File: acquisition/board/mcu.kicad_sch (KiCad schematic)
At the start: 4 parts

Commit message: Continued initial design
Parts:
- gave numbers to parts that had none: 1
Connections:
- net D1V8: now reaches U7.1 (VDD)
- net D1V8: now also U7.17 (VDD), U7.5 (VDDA)
- net GND: now reaches U7.PAD (GND)
- net MCU_SPI_CS_N: now reaches U7.10 (PA4)
- net MCU_SPI_SCK: now reaches U7.11 (PA5)
- net MCU_SPI_SO: now reaches U7.12 (PA6)
- net MCU_SPI_SI: now reaches U7.13 (PA7)
- net ADC0_PDWN: now reaches U7.18 (PA8)
- net ADC1_PDWN: now reaches U7.19 (PA9)
- net ADC2_PDWN: now reaches U7.20 (PA10)
- net ADC3_PDWN: now reaches U7.21 (PA11)
- net PLL_SYNC: now reaches U7.22 (PA12)
- net PLL_SYNC: now also U7.6 (PA0)
- net SWD_SWDIO: now reaches U7.23 (PA13)
- net SWD_SCLK: now reaches U7.24 (PA14)
- net FPGA_INIT_B: now reaches U7.25 (PA15)
- net PLL_STATUS_LD: now reaches U7.7 (PA1)
- net UART_TX: now reaches U7.8 (PA2)
- net UART_TX: now also U7.9 (PA3)
- net PLL_STATUS_HOLDOVER: now reaches U7.14 (PB0)
- net PLL_STATUS_CLKIN0: now reaches U7.15 (PB1)
- net PLL_STATUS_CLKIN1: now reaches U7.16 (PB2)
- net FPGA_RST_N: now reaches U7.26 (PB3)
- net FPGA_DONE: now reaches U7.27 (PB4)
- net LED0: now reaches U7.28 (PB5)
- net LED1: now reaches U7.29 (PB6)
- net LED2: now reaches U7.30 (PB7)
- net LED3: now reaches U7.32 (PB8)
- no-connect marks 0 -> 2
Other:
- note added: "TODO: LEDs"
- note added: "TODO: decoupling"
- note added: "TODO: uart and swd debug headers"
- company: (none) -> A. Zonenberg
- title: (none) -> Digitizer board
- moved on the sheet: U7B, U7C, U7D
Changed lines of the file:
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@@
 (kicad_sch (version 20211123) (generator eeschema)
   (paper "A4")
-  (symbol (lib_id "st-azonenberg:STM32L031-QFN32") (at 101.6 97.79 0) (unit 3)
-    (in_bom yes) (on_board yes) (fields_autoplaced)
-    (property "Reference" "U?" (id 0) (at 117.5512 94.3415 0)
-      (effects (font (size 1.27 1.27)) (justify left))
-    )
-    (property "Value" "STM32L031-QFN32" (id 1) (at 117.5512 97.1166 0)
-      (effects (font (size 1.27 1.27)) (justify left))
-    )
-    (property "Footprint" "" (id 2) (at 101.6 97.79 0)
-      (effects (font (size 1.27 1.27)) hide)
-    )
-    (property "Datasheet" "" (id 3) (at 101.6 97.79 0)
+  (title_block
+    (title "Digitizer board")
+    (date "2022-06-22")
+    (rev "0.1")
+    (company "A. Zonenberg")
+  )
+  (junction (at 36.83 127) (diameter 0) (color 0 0 0 0)
+  )
+  (no_connect (at 36.83 114.3))
+  (no_connect (at 36.83 111.76))
+  (wire (pts (xy 36.83 123.19) (xy 36.83 127))
+    (stroke (width 0) (type default) (color 0 0 0 0))
+  )
+  (wire (pts (xy 36.83 127) (xy 36.83 129.54))
+    (stroke (width 0) (type default) (color 0 0 0 0))
+  )
+  (text "TODO: decoupling" (at 45.72 162.56 0)
+    (effects (font (size 1.27 1.27)) (justify left bottom))
+  )
+  (text "TODO: LEDs" (at 127 87.63 0)
+    (effects (font (size 1.27 1.27)) (justify left bottom))
+  )
+  (text "TODO: uart and swd debug headers" (at 72.39 158.75 0)
+    (effects (font (size 1.27 1.27)) (justify left bottom))
+  )
+  (label "SWD_SWDIO" (at 36.83 64.77 180)
+    (effects (font (size 1.27 1.27)) (justify right bottom))
+  )
+  (label "UART_RX" (at 113.03 55.88 0)
+    (effects (font (size 1.27 1.27)) (justify left bottom))
+  )
+  (label "LED3" (at 116.84 77.47 180)
+    (effects (font (size 1.27 1.27)) (justify right bottom))
+  )
+  (label "LED2" (at 116.84 74.93 180)
+    (effects (font (size 1.27 1.27)) (justify right bottom))
+  )
+  (label "UART_TX" (at 36.83 39.37 180)
+    (effects (font (size 1.27 1.27)) (justify right bottom))
+  )
+  (label "LED0" (at 116.84 69.85 180)
+    (effects (font (size 1.27 1.27)) (justify right bottom))
+  )
+  (label "LED2" (at 36.83 99.06 180)
+    (effects (font (size 1.27 1.27)) (justify right bottom))
+  )
+  (label "UART_TX" (at 36.83 36.83 180)
+    (effects (font (size 1.27 1.27)) (justify right bottom))
+  )
+  (label "LED3" (at 36.83 101.6 180)
+    (effects (font (size 1.27 1.27)) (justify right bottom))
+  )
+  (label "LED0" (at 36.83 93.98 180)
+    (effects (font (size 1.27 1.27)) (justify right bottom))
+  )
+  (label "UART_TX" (at 113.03 53.34 0)
+    (effects (font (size 1.27 1.27)) (justify left bottom))
+  )
+  (label "LED1" (at 116.84 72.39 180)
+    (effects (font (size 1.27 1.27)) (justify right bottom))
+  )
+  (label "SWD_SCLK" (at 36.83 67.31 180)
+    (effects (font (size 1.27 1.27)) (justify right bottom))
+  )
+  (label "LED1" (at 36.83 96.52 180)
+    (effects (font (size 1.27 1.27)) (justify right bottom))
+  )
+  (hierarchical_label "FPGA_DONE" (shape input) (at 36.83 91.44 180)
+    (effects (font (size 1.27 1.27)) (justify right))
+  )
+  (hierarchical_label "PLL_STATUS_LD" (shape input) (at 36.83 34.29 180)
+    (effects (font (size 1.27 1.27)) (justify right))
+  )
+  (hierarchical_label "PLL_SYNC" (shape output) (at 36.83 31.75 180)
+    (effects (font (size 1.27 1.27)) (justify right))
+  )
+  (hierarchical_label "FPGA_RST_N" (shape output) (at 36.83 88.9 180)
+    (effects (font (size 1.27 1.27)) (justify right))
+  )
+  (hierarchical_label "FPGA_INIT_B" (shape bidirectional) (at 36.83 69.85 180)
+    (effects (font (size 1.27 1.27)) (justify right))
+  )
+  (hierarchical_label "ADC0_PDWN" (shape output) (at 36.83 52.07 180)
+    (effects (font (size 1.27 1.27)) (justify right))
+  )
+  (hierarchical_label "ADC2_PDWN" (shape output) (at 36.83 57.15 180)
+    (effects (font (size 1.27 1.27)) (justify right))
+  )
+  (hierarchical_label "D1V8" (shape input) (at 36.83 123.19 180)
+    (effects (font (size 1.27 1.27)) (justify right))
+  )
+  (hierarchical_label "PLL_STATUS_CLKIN0" (shape input) (at 36.83 83.82 180)
+    (effects (font (size 1.27 1.27)) (justify right))
+  )
+  (hierarchical_label "PLL_SYNC" (shape output) (at 36.83 62.23 180)
+    (effects (font (size 1.27 1.27)) (justify right))
+  )
+  (hierarchical_label "MCU_SPI_CS_N" (shape output) (at 36.83 41.91 180)
+    (effects (font (size 1.27 1.27)) (justify right))
+  )
+  (hierarchical_label "PLL_STATUS_HOLDOVER" (shape input) (at 36.83 81.28 180)
+    (effects (font (size 1.27 1.27)) (justify right))
+  )
+  (hierarchical_label "ADC1_PDWN" (shape output) (at 36.83 54.61 180)
+    (effects (font (size 1.27 1.27)) (justify right))
+  )
+  (hierarchical_label "ADC3_PDWN" (shape output) (at 36.83 59.69 180)
+    (effects (font (size 1.27 1.27)) (justify right))
+  )
+  (hierarchical_label "MCU_SPI_SO" (shape input) (at 36.83 46.99 180)
+    (effects (font (size 1.27 1.27)) (justify right))
+  )
+  (hierarchical_label "MCU_SPI_SI" (shape output) (at 36.83 49.53 180)
+    (effects (font (size 1.27 1.27)) (justify right))
+  )
+  (hierarchical_label "MCU_SPI_SCK" (shape output) (at 36.83 44.45 180)
+    (effects (font (size 1.27 1.27)) (justify right))
+  )
+  (hierarchical_label "GND" (shape input) (at 36.83 134.62 180)
+    (effects (font (size 1.27 1.27)) (justify right))
+  )
+  (hierarchical_label "PLL_STATUS_CLKIN1" (shape input) (at 36.83 86.36 180)
+    (effects (font (size 1.27 1.27)) (justify right))
+  )
+  (symbol (lib_id "st-azonenberg:STM32L031-QFN32") (at 40.64 115.57 0) (unit 3)
+    (in_bom yes) (on_board yes)
+    (property "Reference" "U7" (id 0) (at 40.64 116.84 0)
+      (effects (font (size 1.27 1.27)) (justify left))
+    )
+    (property "Value" "STM32L031-QFN32" (id 1) (at 40.64 119.6151 0)
+      (effects (font (size 1.27 1.27)) (justify left))
+    )
+    (property "Footprint" "" (id 2) (at 40.64 115.57 0)
+      (effects (font (size 1.27 1.27)) hide)
+    )
+    (property "Datasheet" "" (id 3) (at 40.64 115.57 0)
       (effects (font (size 1.27 1.27)) hide)
     )
@@
     (pin "3")
   )
-  (symbol (lib_id "st-azonenberg:STM32L031-QFN32") (at 152.4 110.49 0) (unit 4)
-    (in_bom yes) (on_board yes) (fields_autoplaced)
-    (property "Reference" "U?" (id 0) (at 168.3512 98.7865 0)
-      (effects (font (size 1.27 1.27)) (justify left))
-    )
-    (property "Value" "STM32L031-QFN32" (id 1) (at 168.3512 101.5616 0)
-      (effects (font (size 1.27 1.27)) (justify left))
-    )
-    (property "Footprint" "" (id 2) (at 152.4 110.49 0)
-      (effects (font (size 1.27 1.27)) hide)
-    )
-    (property "Datasheet" "" (id 3) (at 152.4 110.49 0)
+  (symbol (lib_id "st-azonenberg:STM32L031-QFN32") (at 40.64 143.51 0) (unit 4)
+    (in_bom yes) (on_board yes)
+    (property "Reference" "U7" (id 0) (at 40.64 145.415 0)
+      (effects (font (size 1.27 1.27)) (justify left))
+    )
+    (property "Value" "STM32L031-QFN32" (id 1) (at 40.64 148.1901 0)
+      (effects (font (size 1.27 1.27)) (justify left))
+    )
+    (property "Footprint" "" (id 2) (at 40.64 143.51 0)
+      (effects (font (size 1.27 1.27)) hide)
+    )
+    (property "Datasheet" "" (id 3) (at 40.64 143.51 0)
       (effects (font (size 1.27 1.27)) hide)
     )
@@
   )
   (symbol (lib_id "st-azonenberg:STM32L031-QFN32") (at 40.64 71.12 0) (unit 1)
-    (in_bom yes) (on_board yes) (fields_autoplaced)
-    (property "Reference" "U?" (id 0) (at 56.5912 49.8915 0)
-      (effects (font (size 1.27 1.27)) (justify left))
-    )
-    (property "Value" "STM32L031-QFN32" (id 1) (at 56.5912 52.6666 0)
+    (in_bom yes) (on_board yes)
+    (property "Reference" "U7" (id 0) (at 40.64 72.1549 0)
+      (effects (font (size 1.27 1.27)) (justify left))
+    )
+    (property "Value" "STM32L031-QFN32" (id 1) (at 40.64 74.93 0)
       (effects (font (size 1.27 1.27)) (justify left))
     )
@@
       (effects (font (size 1.27 1.27)) hide)
     )
-    (pin "10")
-    (pin "11")
-    (pin "12")
-    (pin "13")
+    (pin "10" (alternate "SPI1_NSS"))
+    (pin "11" (alternate "SPI1_SCK"))
+    (pin "12" (alternate "SPI1_MISO"))
+    (pin "13" (alternate "SPI1_MOSI"))
     (pin "18")
     (pin "19")
@@
     (pin "21")
     (pin "22")
-    (pin "23")
-    (pin "24")
+    (pin "23" (alternate "SWDIO"))
+    (pin "24" (alternate "SWCLK"))
     (pin "25")
     (pin "6")
     (pin "7")
-    (pin "8")
-    (pin "9")
-  )
-  (symbol (lib_id "st-azonenberg:STM32L031-QFN32") (at 72.39 86.36 0) (unit 2)
-    (in_bom yes) (on_board yes) (fields_autoplaced)
-    (property "Reference" "U?" (id 0) (at 88.3412 74.0215 0)
-      (effects (font (size 1.27 1.27)) (justify left))
-    )
-    (property "Value" "STM32L031-QFN32" (id 1) (at 88.3412 76.7966 0)
-      (effects (font (size 1.27 1.27)) (justify left))
-    )
-    (property "Footprint" "" (id 2) (at 72.39 86.36 0)
-      (effects (font (size 1.27 1.27)) hide)
-    )
-    (property "Datasheet" "" (id 3) (at 72.39 86.36 0)
-      (effects (font (size 1.27 1.27)) hide)
-    )
+    (pin "8" (alternate "USART2_TX"))
+    (pin "9" (alternate "USART2_RX"))
+  )
+  (symbol (lib_id "st-azonenberg:STM32L031-QFN32") (at 40.64 102.87 0) (unit 2)
+    (in_bom yes) (on_board yes)
+    (property "Reference" "U7" (id 0) (at 40.64 103.9049 0)
+      (effects (font (size 1.27 1.27)) (justify left))
+    )
+    (property "Value" "STM32L031-QFN32" (id 1) (at 40.64 106.68 0)
+      (effects (font (size 1.27 1.27)) (justify left))
+    )
+    (property "Footprint" "" (id 2) (at 40.64 102.87 0)
+      (effects (font (size 1.27 1.27)) hide)
+    )
+    (property "Datasheet" "" (id 3) (at 40.64 102.87 0)
+      (effects (font (size 1.27 1.27)) hide)
+    )

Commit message: Updated schematic with a lot of level shifting and support stuff, power decoupling, etc. Almost done except power supply and protection diodes
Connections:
- net PLL_STATUS_CLKIN0: no longer names the net of U7.15 (PB1)
- net PLL_STATUS_CLKIN1: no longer names the net of U7.16 (PB2)
- net PLL_STATUS_HOLDOVER: no longer names the net of U7.14 (PB0)
- no-connect marks 2 -> 5
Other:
- note added: "FIXME: LEDs need level shifting FETs for 1.8V drive"
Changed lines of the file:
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@@
   (title_block
     (title "Digitizer board")
-    (date "2022-06-22")
+    (date "2022-07-04")
     (rev "0.1")
     (company "A. Zonenberg")
@@
   )
   (no_connect (at 36.83 114.3))
+  (no_connect (at 36.83 86.36))
+  (no_connect (at 36.83 83.82))
+  (no_connect (at 36.83 81.28))
   (no_connect (at 36.83 111.76))
   (wire (pts (xy 36.83 123.19) (xy 36.83 127))
@@
   )
   (text "TODO: decoupling" (at 45.72 162.56 0)
+    (effects (font (size 1.27 1.27)) (justify left bottom))
+  )
+  (text "FIXME: LEDs need level shifting FETs for 1.8V drive"
+    (at 123.19 95.25 0)
     (effects (font (size 1.27 1.27)) (justify left bottom))
   )
@@
     (effects (font (size 1.27 1.27)) (justify right))
   )
-  (hierarchical_label "PLL_STATUS_CLKIN0" (shape input) (at 36.83 83.82 180)
-    (effects (font (size 1.27 1.27)) (justify right))
-  )
   (hierarchical_label "PLL_SYNC" (shape output) (at 36.83 62.23 180)
     (effects (font (size 1.27 1.27)) (justify right))
   )
   (hierarchical_label "MCU_SPI_CS_N" (shape output) (at 36.83 41.91 180)
-    (effects (font (size 1.27 1.27)) (justify right))
-  )
-  (hierarchical_label "PLL_STATUS_HOLDOVER" (shape input) (at 36.83 81.28 180)
     (effects (font (size 1.27 1.27)) (justify right))
   )
@@
     (effects (font (size 1.27 1.27)) (justify right))
   )
-  (hierarchical_label "PLL_STATUS_CLKIN1" (shape input) (at 36.83 86.36 180)
-    (effects (font (size 1.27 1.27)) (justify right))
-  )

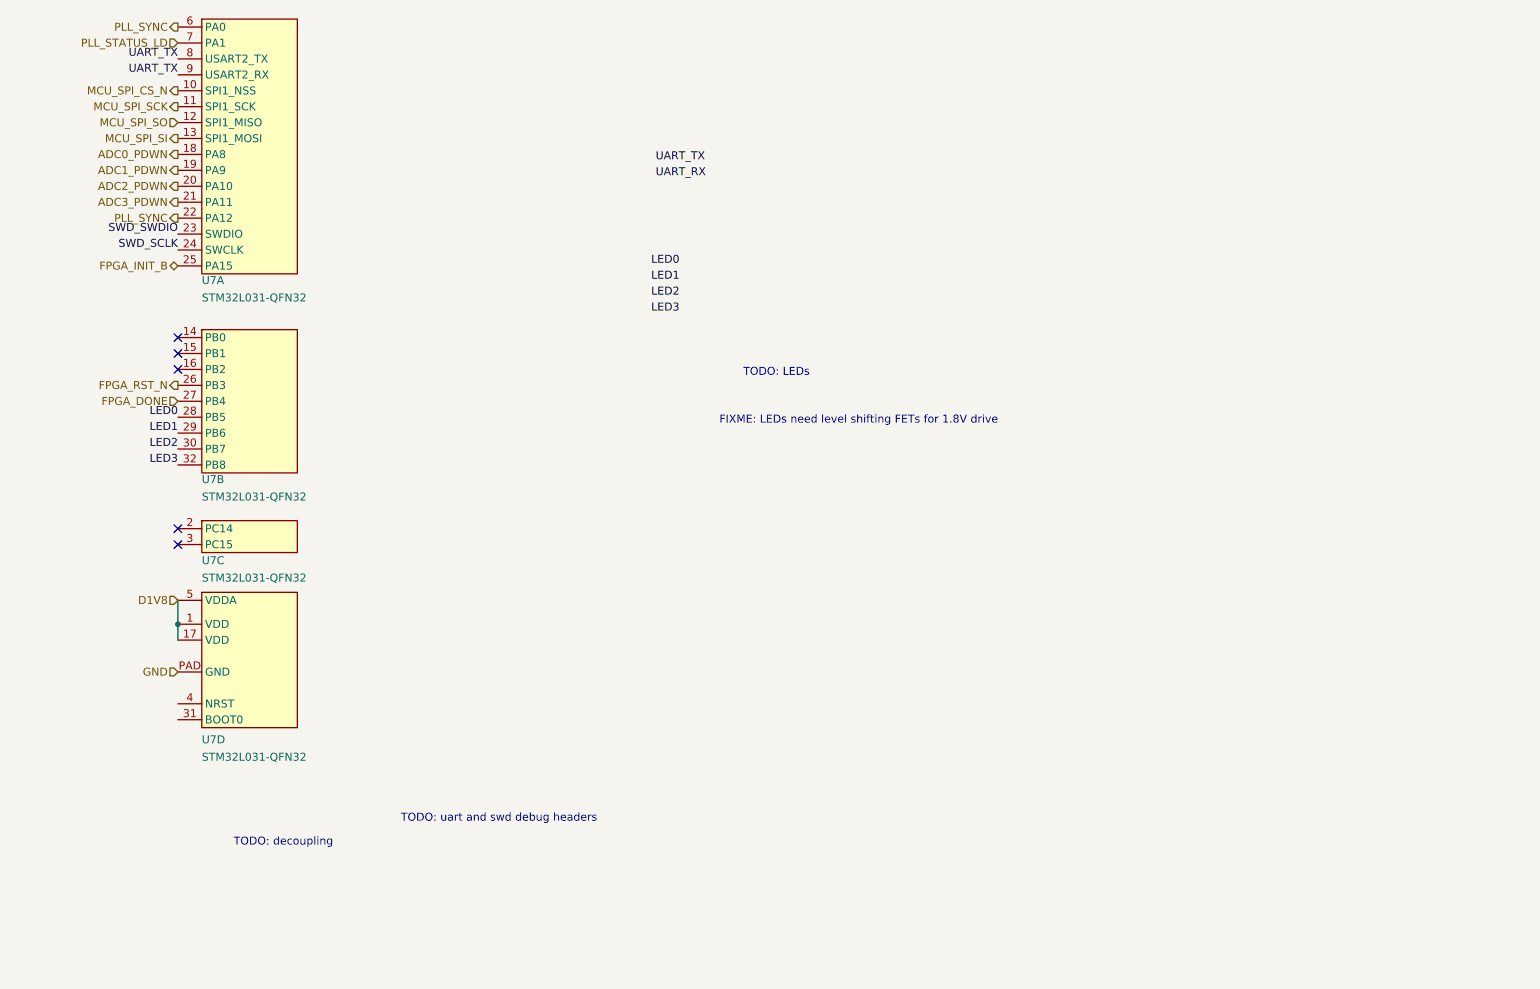
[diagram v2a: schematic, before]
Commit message: Lots of progress on power supply design, added a bunch of test points, etc
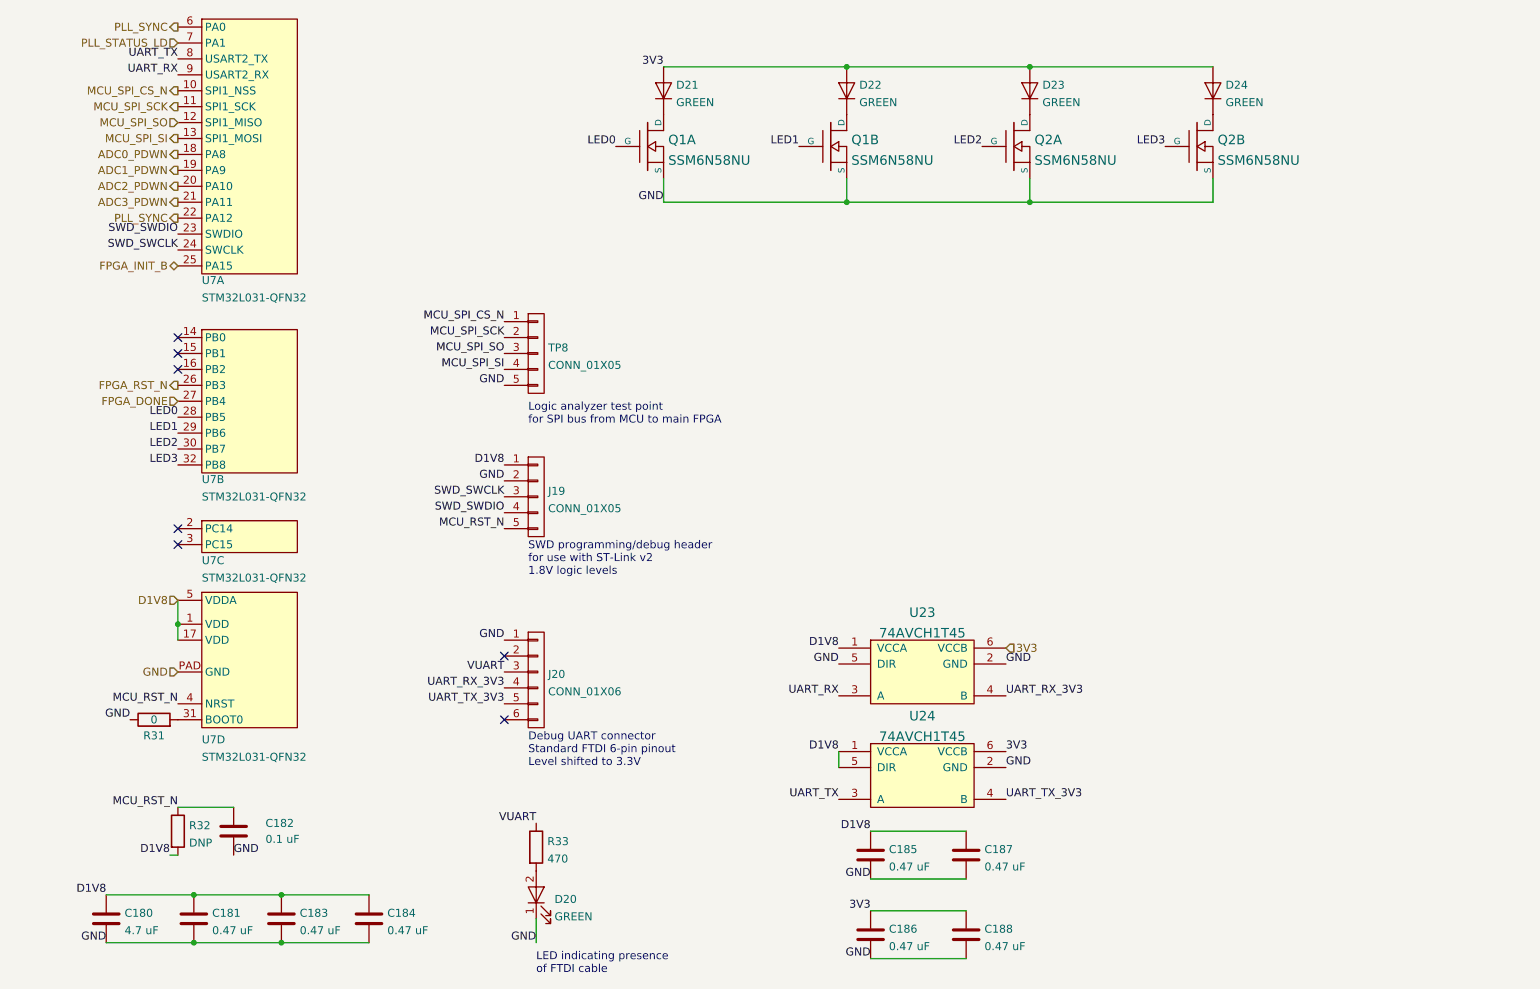
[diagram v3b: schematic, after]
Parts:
- added C180: 4.7 uF, symbol device:C
- added C181, C183, C184, C185, C186, C187, C188: 0.47 uF, symbol device:C
- added C182: 0.1 uF, symbol device:C
- added D20: GREEN, symbol device:LED
- added D21, D22, D23, D24: GREEN, symbol device:D
- added J19, TP8: CONN_01X05, symbol conn:CONN_01X05
- added J20: CONN_01X06, symbol conn:CONN_01X06
- added Q1, Q2: SSM6N58NU, symbol special-azonenberg:SSM6N58NU_DUAL_NMOS
- added R31: 0, symbol device:R
- added R32: DNP, symbol device:R
- added R33: 470, symbol device:R
- added U23, U24: 74AVCH1T45, symbol special-azonenberg:74LVC1T45
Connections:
- net D1V8: now also C180.1, C181.1, C183.1, C184.1, C185.1, C187.1, J19.1 (P1), R32.2, U23.1 (VCCA), U24.1 (VCCA), U24.5 (DIR)
- net GND: now also C180.2, C181.2, C182.2, C183.2, C184.2, C185.2, C186.2, C187.2, C188.2, D20.1 (K), J19.2 (P2), J20.1 (P1), Q1.S1 (S), Q1.S2 (S), Q2.S1 (S), Q2.S2 (S), R31.1, TP8.5 (P5), U23.2 (GND), U23.5 (DIR), U24.2 (GND)
- net LED0: now also Q1.G1 (G)
- net LED1: now also Q1.G2 (G)
- net LED2: now also Q2.G1 (G)
- net LED3: now also Q2.G2 (G)
- net MCU_SPI_CS_N: now also TP8.1 (P1)
- net MCU_SPI_SCK: now also TP8.2 (P2)
- net MCU_SPI_SI: now also TP8.4 (P4)
- net MCU_SPI_SO: now also TP8.3 (P3)
- net SWD_SWDIO: now also J19.4 (P4)
- net UART_RX: now also U7.9 (PA3), U23.3 (A)
- net UART_TX: now also U24.3 (A); no longer U7.9 (PA3)
- net at U7.31 (BOOT0): now also R31.2
- net MCU_RST_N: now reaches U7.4 (NRST)
- net MCU_RST_N: now also C182.1, J19.5 (P5), R32.1
- net SWD_SCLK renamed SWD_SWCLK
- net SWD_SWCLK: now also J19.3 (P3)
- new net: D20.2 (A), R33.2
- new net: D22.1 (K), Q1.D2 (D)
- new net: D21.1 (K), Q1.D1 (D)
- new net: D24.1 (K), Q2.D2 (D)
- new net: D23.1 (K), Q2.D1 (D)
- new net 3V3: C186.1, C188.1, D21.2 (A), D22.2 (A), D23.2 (A), D24.2 (A), U23.6 (VCCB), U24.6 (VCCB)
- new net UART_RX_3V3: J20.4 (P4), U23.4 (B)
- new net UART_TX_3V3: J20.5 (P5), U24.4 (B)
- new net VUART: J20.3 (P3), R33.1
- no-connect marks 5 -> 7
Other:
- note added: "Debug UART connector Standard FTDI 6-pin pinout Level shifted to 3.3V"
- note added: "LED indicating presence of FTDI cable"
- note added: "Logic analyzer test point for SPI bus from MCU to main FPGA"
- note added: "SWD programming/debug header for use with ST-Link v2 1.8V logic levels"
- note removed: "FIXME: LEDs need level shifting FETs for 1.8V drive"
- note removed: "TODO: LEDs"
- note removed: "TODO: decoupling"
- note removed: "TODO: uart and swd debug headers"
